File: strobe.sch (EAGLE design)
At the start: 59 parts, among them IC1 AT90USB162A, Q1 IRF3704S, Q2 IRF3704S, Q4 IRF3704S, Q5 IRF3704S, T1 BC849, T2 BC849, T3 BC849, T4 BC849, T5 BC849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

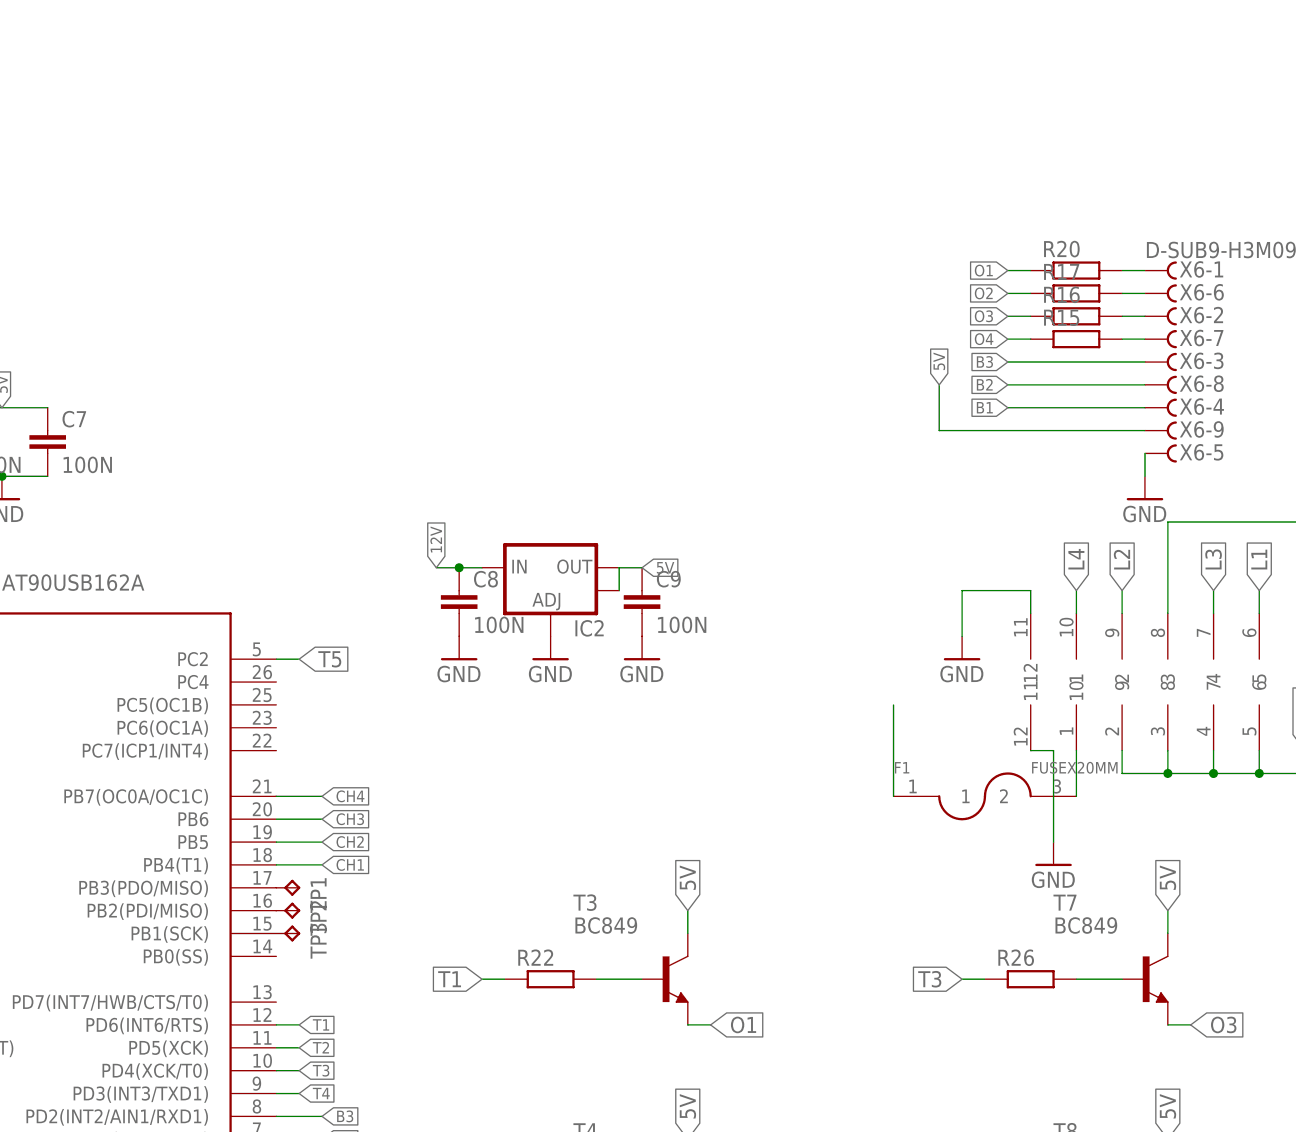
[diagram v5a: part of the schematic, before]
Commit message: bezpiecznik out
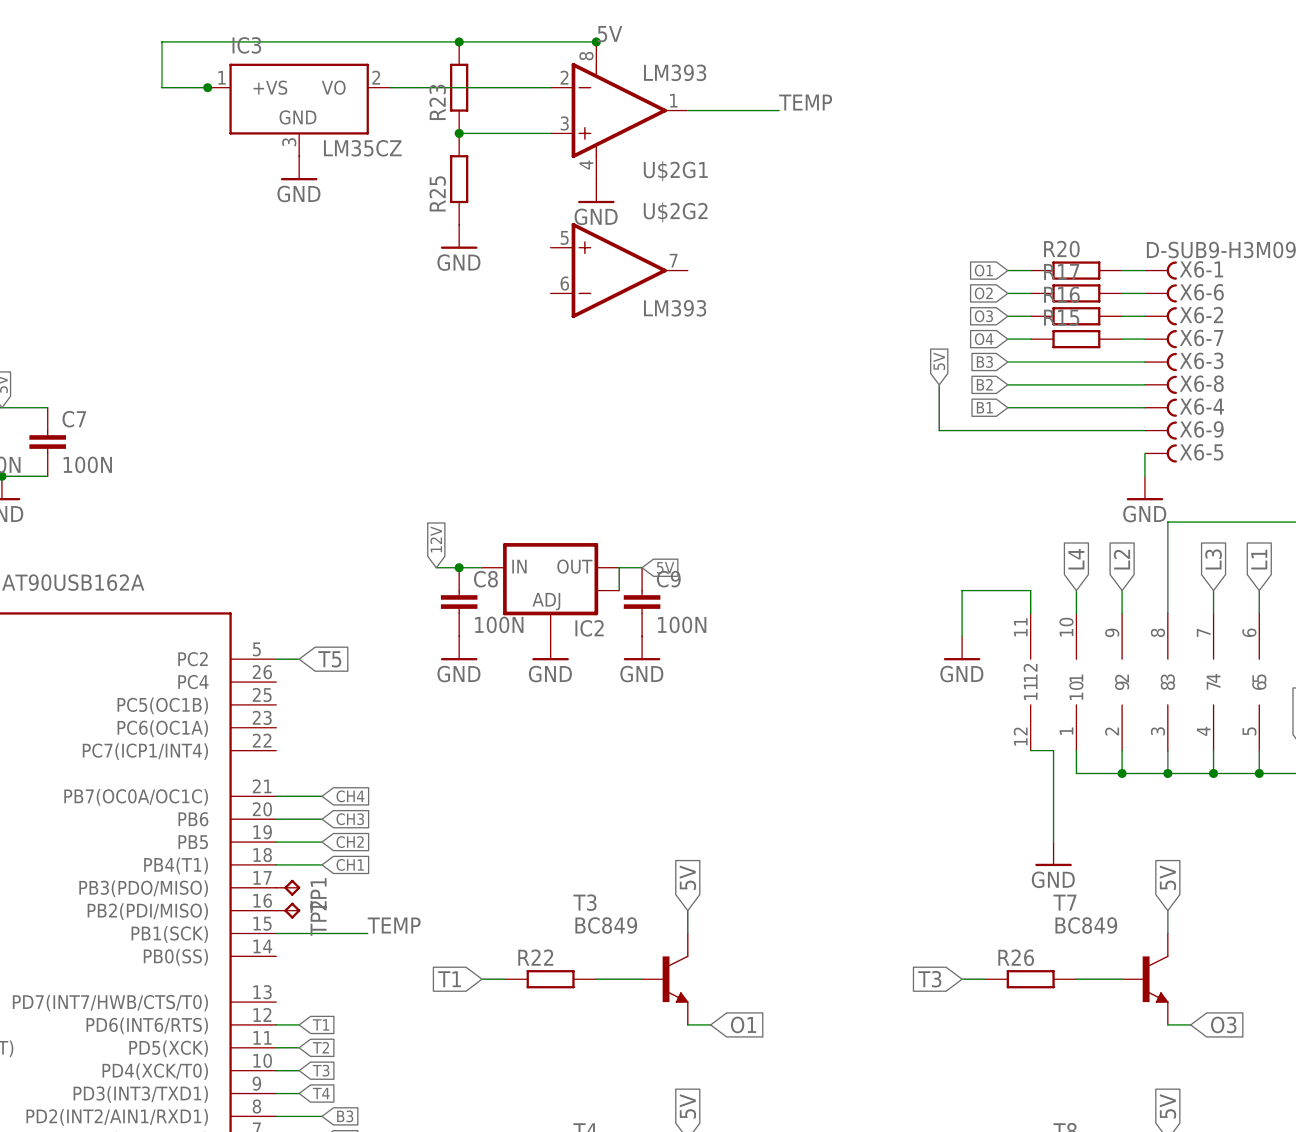
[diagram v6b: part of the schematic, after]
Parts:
- removed F1: FUSEX20MM, SparkFun-Passives:FUSEX20MM
- removed TP3: TPB1,27, testpad:TPB1,27
- added IC3: LM35CZ, lm35:LM35CZ
- added R23, R25: (no value), rcl:R-EU_M0805
- added U$2: LM393, SparkFun-AnalogIC:LM393
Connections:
- removed net N$32: IC1.PB1(SCK), TP3.TP
- new net N$4: R23.1, R25.2, U$2G1.+IN
- new net TEMP: IC1.PB1(SCK), U$2G1.OUT
- net 12V: now also U$1.1; no longer F1.1
- net 5V: now also IC3.+VS, R23.2, U$2G1.V+
- net GND: now also IC3.GND, R25.1, U$2G1.V-
- net N$3: now also IC3.VO, U$2G1.-IN; no longer F1.2, U$1.1
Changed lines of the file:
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@@
 <part name="TP1" library="testpad" deviceset="TP" device="B1,27"/>
 <part name="TP2" library="testpad" deviceset="TP" device="B1,27"/>
-<part name="TP3" library="testpad" deviceset="TP" device="B1,27"/>
 <part name="TP4" library="testpad" deviceset="TP" device="B1,27"/>
 <part name="LED6" library="led" deviceset="LED" device="SML0805"/>
@@
 <part name="U$1" library="con-amphenol" deviceset="MF42-10" device=""/>
 <part name="GND6" library="SparkFun-Aesthetics" deviceset="GND" device=""/>
-<part name="F1" library="SparkFun-Passives" deviceset="FUSE" device="X20MM"/>
 <part name="GND17" library="SparkFun-Aesthetics" deviceset="GND" device=""/>
 <part name="GND18" library="SparkFun-Aesthetics" deviceset="GND" device=""/>
+<part name="U$2" library="SparkFun-AnalogIC" deviceset="LM393" device=""/>
+<part name="GND19" library="SparkFun-Aesthetics" deviceset="GND" device=""/>
+<part name="IC3" library="lm35" deviceset="LM35" device="CZ"/>
+<part name="R23" library="rcl" deviceset="R-EU_" device="M0805"/>
+<part name="R25" library="rcl" deviceset="R-EU_" device="M0805"/>
+<part name="GND20" library="SparkFun-Aesthetics" deviceset="GND" device=""/>
+<part name="GND25" library="SparkFun-Aesthetics" deviceset="GND" device=""/>
 </parts>
 <sheets>
@@
 <instance part="TP1" gate="G$1" x="73.66" y="147.32" rot="R270"/>
 <instance part="TP2" gate="G$1" x="73.66" y="144.78" rot="R270"/>
-<instance part="TP3" gate="G$1" x="73.66" y="142.24" rot="R270"/>
 <instance part="TP4" gate="G$1" x="20.32" y="132.08"/>
 <instance part="LED6" gate="G$1" x="-2.54" y="205.74" rot="R270"/>
@@
 <instance part="U$1" gate="G$1" x="170.18" y="170.18"/>
 <instance part="GND6" gate="1" x="187.96" y="180.34"/>
-<instance part="F1" gate="G$1" x="149.86" y="157.48"/>
 <instance part="GND17" gate="1" x="157.48" y="149.86"/>
 <instance part="GND18" gate="1" x="147.32" y="172.72"/>
+<instance part="U$2" gate="G1" x="106.68" y="233.68"/>
+<instance part="U$2" gate="G2" x="109.22" y="215.9"/>
+<instance part="GND19" gate="1" x="106.68" y="223.52"/>
+<instance part="IC3" gate="G$1" x="73.66" y="236.22"/>
+<instance part="R23" gate="G$1" x="91.44" y="236.22" rot="R90"/>
+<instance part="R25" gate="G$1" x="91.44" y="226.06" rot="R90"/>
+<instance part="GND20" gate="1" x="91.44" y="218.44"/>
+<instance part="GND25" gate="1" x="73.66" y="226.06"/>
 </instances>
 <busses>
@@
 <wire x1="147.32" y1="180.34" x2="147.32" y2="175.26" width="0.1524" layer="91"/>
 <pinref part="GND18" gate="1" pin="GND"/>
+</segment>
+<segment>
+<pinref part="U$2" gate="G1" pin="V-"/>
+<pinref part="GND19" gate="1" pin="GND"/>
+</segment>
+<segment>
+<pinref part="R25" gate="G$1" pin="1"/>
+<pinref part="GND20" gate="1" pin="GND"/>
+</segment>
+<segment>
+<pinref part="IC3" gate="G$1" pin="GND"/>
+<pinref part="GND25" gate="1" pin="GND"/>
 </segment>
 </net>
@@
 <label x="144.78" y="203.2" size="1.27" layer="95" rot="R90" xref="yes"/>
 </segment>
+<segment>
+<pinref part="IC3" gate="G$1" pin="+VS"/>
+<wire x1="63.5" y1="236.22" x2="58.42" y2="236.22" width="0.1524" layer="91"/>
+<wire x1="58.42" y1="236.22" x2="58.42" y2="241.3" width="0.1524" layer="91"/>
+<pinref part="U$2" gate="G1" pin="V+"/>
+<wire x1="58.42" y1="241.3" x2="91.44" y2="241.3" width="0.1524" layer="91"/>
+<pinref part="R23" gate="G$1" pin="2"/>
+<junction x="91.44" y="241.3"/>
+<wire x1="91.44" y1="241.3" x2="106.68" y2="241.3" width="0.1524" layer="91"/>
+<junction x="106.68" y="241.3"/>
+<junction x="63.5" y="236.22"/>
+<label x="106.68" y="241.3" size="1.778" layer="95"/>
+</segment>
 </net>
 <net name="N$10" class="0">
@@
 <junction x="180.34" y="160.02"/>
 <label x="185.42" y="162.56" size="1.778" layer="95" rot="R90" xref="yes"/>
-</segment>
-<segment>
-<pinref part="F1" gate="G$1" pin="1"/>
-<wire x1="139.7" y1="157.48" x2="139.7" y2="167.64" width="0.1524" layer="91"/>
+<pinref part="U$1" gate="G$1" pin="1"/>
+<wire x1="160.02" y1="162.56" x2="160.02" y2="160.02" width="0.1524" layer="91"/>
+<wire x1="160.02" y1="160.02" x2="165.1" y2="160.02" width="0.1524" layer="91"/>
+<junction x="165.1" y="160.02"/>
 </segment>
 </net>
@@
 </segment>
 </net>
-<net name="N$32" class="0">
-<segment>
-<pinref part="IC1" gate="G$1" pin="PB1(SCK)"/>
-<pinref part="TP3" gate="G$1" pin="TP"/>
-</segment>
-</net>
 <net name="N$23" class="0">
 <segment>
@@
 <net name="N$3" class="0">
 <segment>
-<pinref part="U$1" gate="G$1" pin="1"/>
-<pinref part="F1" gate="G$1" pin="2"/>
-<wire x1="160.02" y1="157.48" x2="160.02" y2="162.56" width="0.1524" layer="91"/>
-</segment>
-</net>
+<pinref part="IC3" gate="G$1" pin="VO"/>
+<pinref part="U$2" gate="G1" pin="-IN"/>
+<wire x1="83.82" y1="236.22" x2="101.6" y2="236.22" width="0.1524" layer="91"/>
+</segment>
+</net>
+<net name="N$4" class="0">
+<segment>
+<pinref part="R23" gate="G$1" pin="1"/>
+<pinref part="R25" gate="G$1" pin="2"/>
+<pinref part="U$2" gate="G1" pin="+IN"/>
+<wire x1="101.6" y1="231.14" x2="91.44" y2="231.14" width="0.1524" layer="91"/>
+<junction x="91.44" y="231.14"/>
+</segment>
+</net>
+<net name="TEMP" class="0">
+<segment>
+<pinref part="IC1" gate="G$1" pin="PB1(SCK)"/>
+<wire x1="71.12" y1="142.24" x2="81.28" y2="142.24" width="0.1524" layer="91"/>
+<label x="81.28" y="142.24" size="1.778" layer="95"/>
+</segment>
+<segment>
+<pinref part="U$2" gate="G1" pin="OUT"/>
+<wire x1="116.84" y1="233.68" x2="127" y2="233.68" width="0.1524" layer="91"/>
+<label x="127" y="233.68" size="1.778" layer="95"/>
+</segment>
+</net>

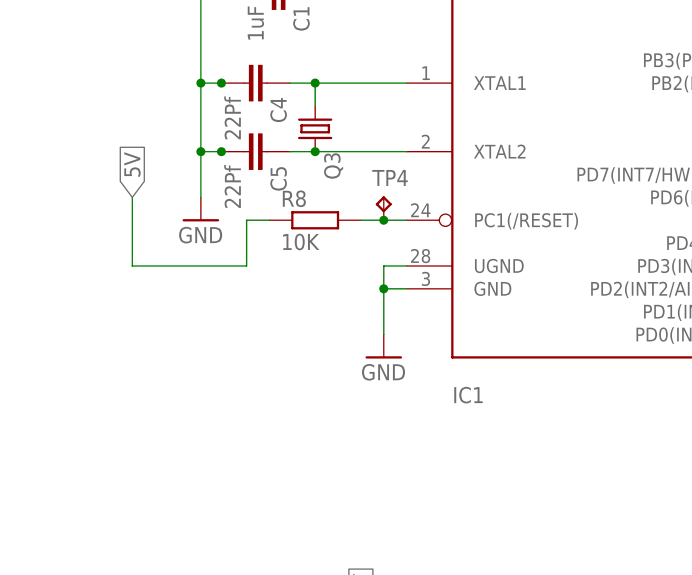
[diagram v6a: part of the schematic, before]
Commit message: dodany reset na goldpinach, poprawka przelotki
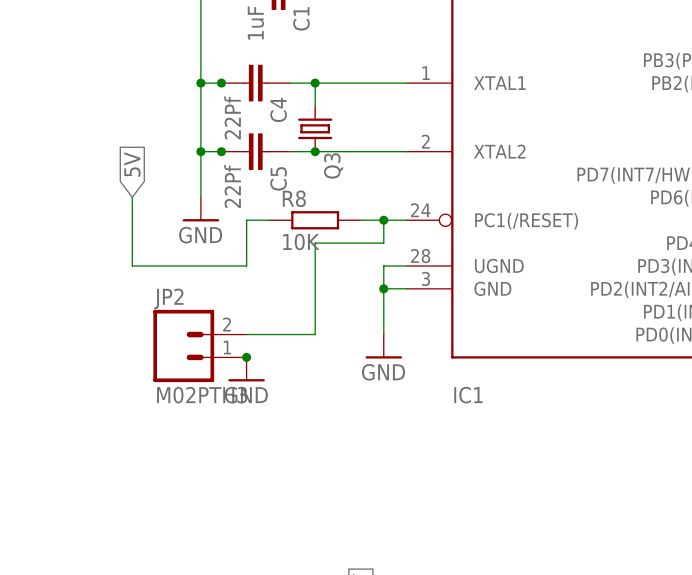
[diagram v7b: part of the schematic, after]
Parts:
- removed TP4: TPB1,27, testpad:TPB1,27
- added JP2: M02PTH3, SparkFun-Connectors:M02PTH3
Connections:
- net GND: now also JP2.1
- net N$14: now also JP2.2; no longer TP4.TP
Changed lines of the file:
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@@
 <part name="TP1" library="testpad" deviceset="TP" device="B1,27"/>
 <part name="TP2" library="testpad" deviceset="TP" device="B1,27"/>
-<part name="TP4" library="testpad" deviceset="TP" device="B1,27"/>
 <part name="LED6" library="led" deviceset="LED" device="SML0805"/>
 <part name="R21" library="rcl" deviceset="R-EU_" device="R0805" value="340"/>
@@
 <part name="GND20" library="SparkFun-Aesthetics" deviceset="GND" device=""/>
 <part name="GND25" library="SparkFun-Aesthetics" deviceset="GND" device=""/>
+<part name="JP2" library="SparkFun-Connectors" deviceset="M02" device="PTH3"/>
+<part name="GND26" library="SparkFun-Aesthetics" deviceset="GND" device=""/>
 </parts>
 <sheets>
@@
 <instance part="TP1" gate="G$1" x="73.66" y="147.32" rot="R270"/>
 <instance part="TP2" gate="G$1" x="73.66" y="144.78" rot="R270"/>
-<instance part="TP4" gate="G$1" x="20.32" y="132.08"/>
 <instance part="LED6" gate="G$1" x="-2.54" y="205.74" rot="R270"/>
 <instance part="R21" gate="G$1" x="5.08" y="205.74" rot="R180"/>
@@
 <instance part="GND20" gate="1" x="91.44" y="218.44"/>
 <instance part="GND25" gate="1" x="73.66" y="226.06"/>
+<instance part="JP2" gate="G$1" x="-2.54" y="114.3"/>
+<instance part="GND26" gate="1" x="5.08" y="111.76"/>
 </instances>
 <busses>
@@
 <pinref part="IC3" gate="G$1" pin="GND"/>
 <pinref part="GND25" gate="1" pin="GND"/>
+</segment>
+<segment>
+<pinref part="JP2" gate="G$1" pin="1"/>
+<pinref part="GND26" gate="1" pin="GND"/>
+<junction x="5.08" y="114.3"/>
 </segment>
 </net>
@@
 <segment>
 <pinref part="IC1" gate="G$1" pin="PC1(/RESET)"/>
+<pinref part="R8" gate="G$1" pin="2"/>
 <wire x1="22.86" y1="129.54" x2="20.32" y2="129.54" width="0.1524" layer="91"/>
-<pinref part="R8" gate="G$1" pin="2"/>
-<pinref part="TP4" gate="G$1" pin="TP"/>
 <wire x1="20.32" y1="129.54" x2="17.78" y2="129.54" width="0.1524" layer="91"/>
+<wire x1="20.32" y1="129.54" x2="20.32" y2="127" width="0.1524" layer="91"/>
+<wire x1="20.32" y1="127" x2="12.7" y2="127" width="0.1524" layer="91"/>
+<wire x1="12.7" y1="127" x2="12.7" y2="116.84" width="0.1524" layer="91"/>
+<pinref part="JP2" gate="G$1" pin="2"/>
+<wire x1="12.7" y1="116.84" x2="5.08" y2="116.84" width="0.1524" layer="91"/>
 <junction x="20.32" y="129.54"/>
 </segment>
